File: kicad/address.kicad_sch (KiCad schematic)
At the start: 11 parts, among them J1 VLB_slot, U1 86C325, U8 7404, U9 7408

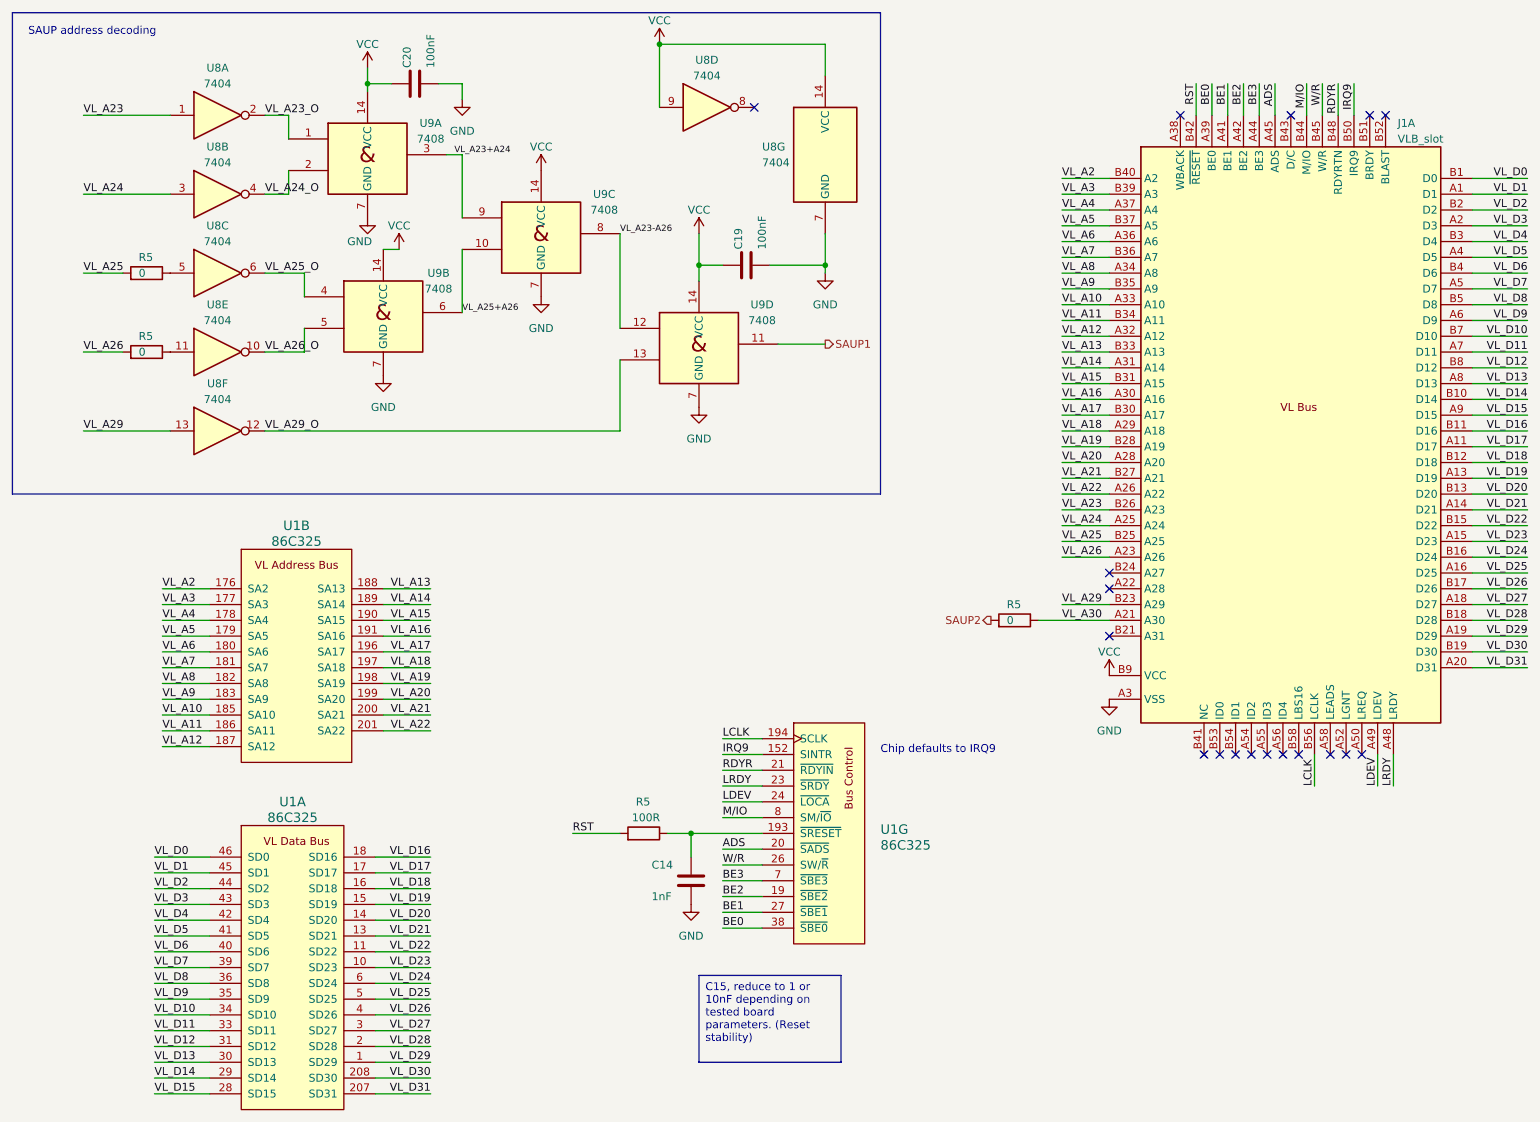
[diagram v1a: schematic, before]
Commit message: some optimizations and silkscreen updating
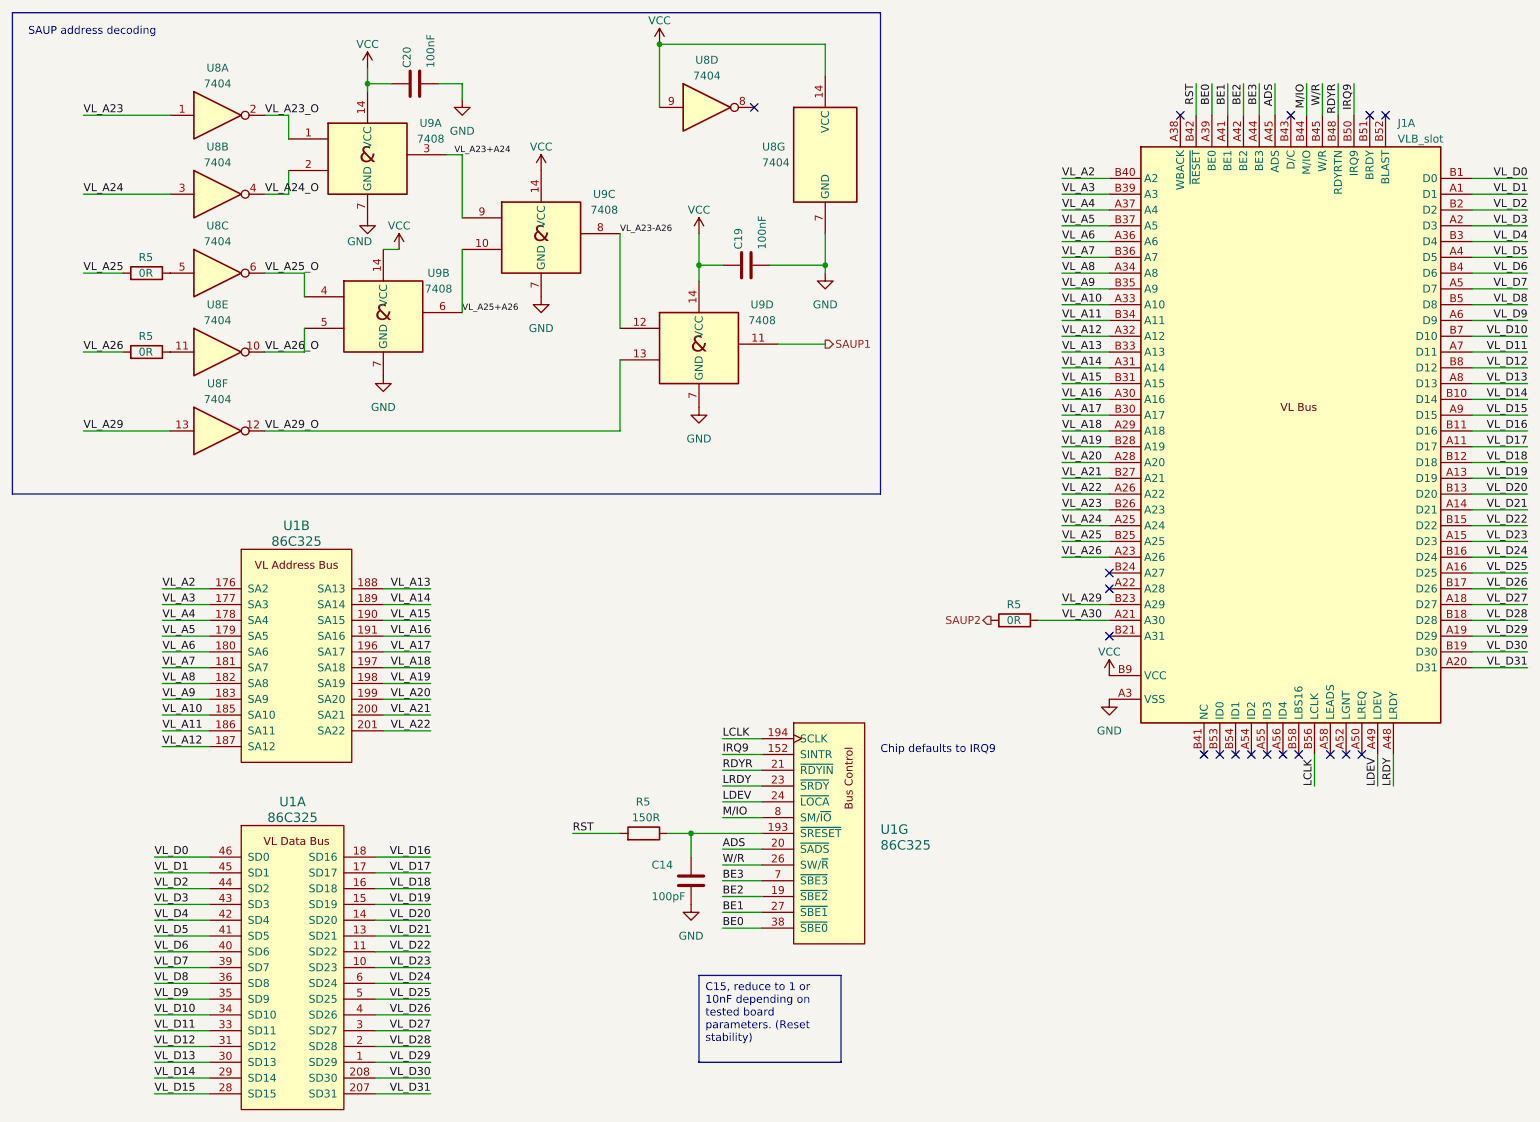
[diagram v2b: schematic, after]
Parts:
- C14: value 1nF -> 100pF
- J1: now left out of the parts list
- R5: value 100R -> 150R
- R5: value 0 -> 0R
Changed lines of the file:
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@@
       (effects (font (size 1.27 1.27)) (justify left))
     )
-    (property "Value" "100R" (at 116.205 144.78 90)
+    (property "Value" "150R" (at 116.205 144.78 90)
       (effects (font (size 1.27 1.27)) (justify left))
     )
@@
         )
         (path "/e8216711-86b5-4276-82f4-4c7ed22b9a9c/9321f466-5ac6-411a-b039-07fb7f0cdeaa"
-          (reference "R45") (unit 1)
+          (reference "R47") (unit 1)
         )
       )
@@
       (effects (font (size 1.27 1.27)) (justify left))
     )
-    (property "Value" "0" (at 36.83 69.85 90)
+    (property "Value" "0R" (at 36.83 69.85 90)
       (effects (font (size 1.27 1.27)) (justify left))
     )
@@
         )
         (path "/e8216711-86b5-4276-82f4-4c7ed22b9a9c/9321f466-5ac6-411a-b039-07fb7f0cdeaa"
-          (reference "R48") (unit 1)
+          (reference "R7") (unit 1)
         )
       )
@@
       (effects (font (size 1.27 1.27)) (justify left))
     )
-    (property "Value" "0" (at 36.83 57.15 90)
+    (property "Value" "0R" (at 36.83 57.15 90)
       (effects (font (size 1.27 1.27)) (justify left))
     )
@@
         )
         (path "/e8216711-86b5-4276-82f4-4c7ed22b9a9c/9321f466-5ac6-411a-b039-07fb7f0cdeaa"
-          (reference "R47") (unit 1)
+          (reference "R6") (unit 1)
         )
       )
@@
       (effects (font (size 1.27 1.27)) (justify left))
     )
-    (property "Value" "1nF" (at 119.38 157.48 0)
+    (property "Value" "100pF" (at 119.38 157.48 0)
       (effects (font (size 1.27 1.27)) (justify left))
     )
@@
       (effects (font (size 1.27 1.27)) (justify left))
     )
-    (property "Value" "0" (at 176.53 113.03 90)
+    (property "Value" "0R" (at 176.53 113.03 90)
       (effects (font (size 1.27 1.27)) (justify left))
     )
@@
         )
         (path "/e8216711-86b5-4276-82f4-4c7ed22b9a9c/9321f466-5ac6-411a-b039-07fb7f0cdeaa"
-          (reference "R49") (unit 1)
+          (reference "R8") (unit 1)
         )
       )
@@
   )
   (symbol (lib_id "virge:VLB_slot") (at 219.71 77.47 0) (unit 1)
-    (in_bom yes) (on_board yes) (dnp no)
+    (in_bom no) (on_board yes) (dnp no)
     (property "Reference" "J1" (at 239.4459 33.02 0)
       (effects (font (size 1.27 1.27)) (justify left))

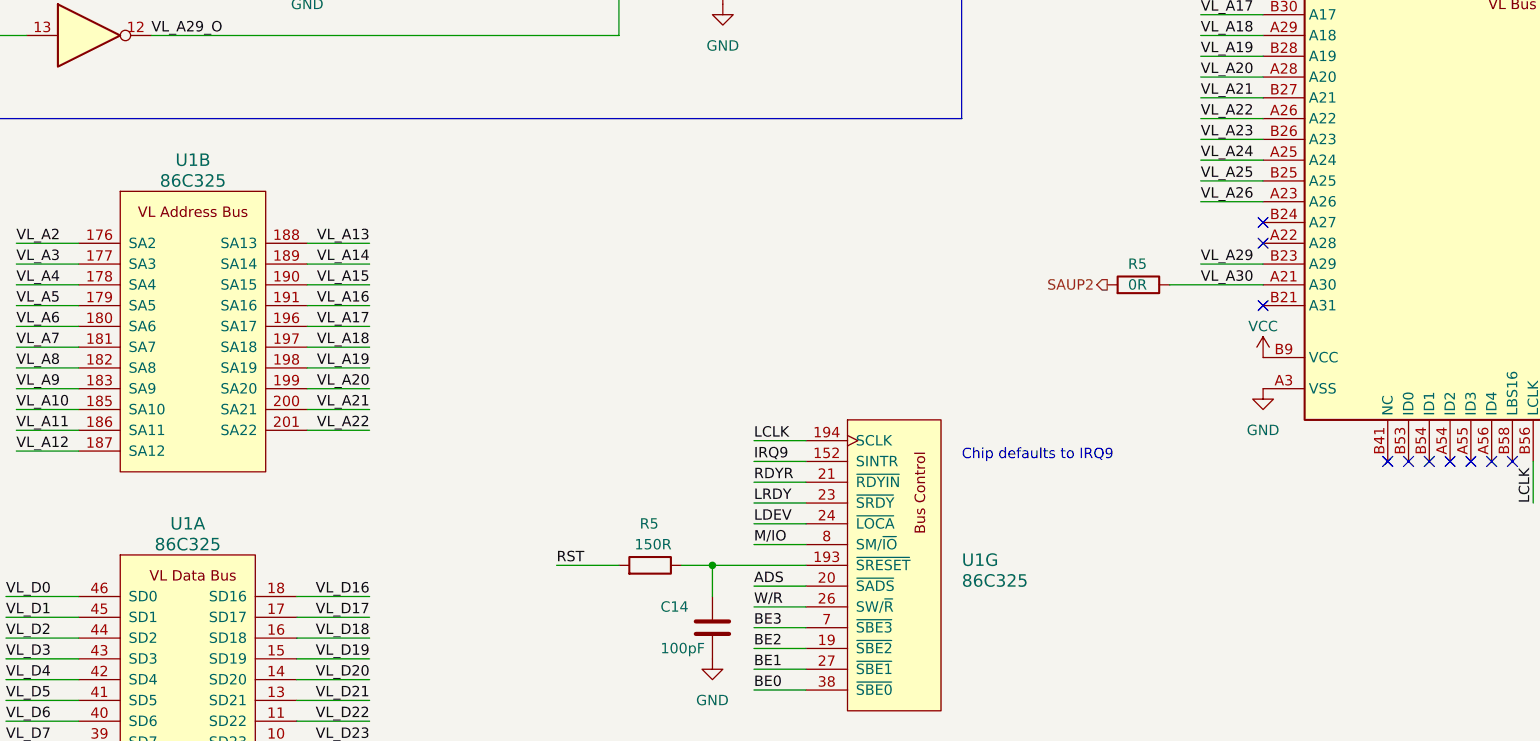
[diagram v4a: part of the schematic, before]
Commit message: updated VLB footprint
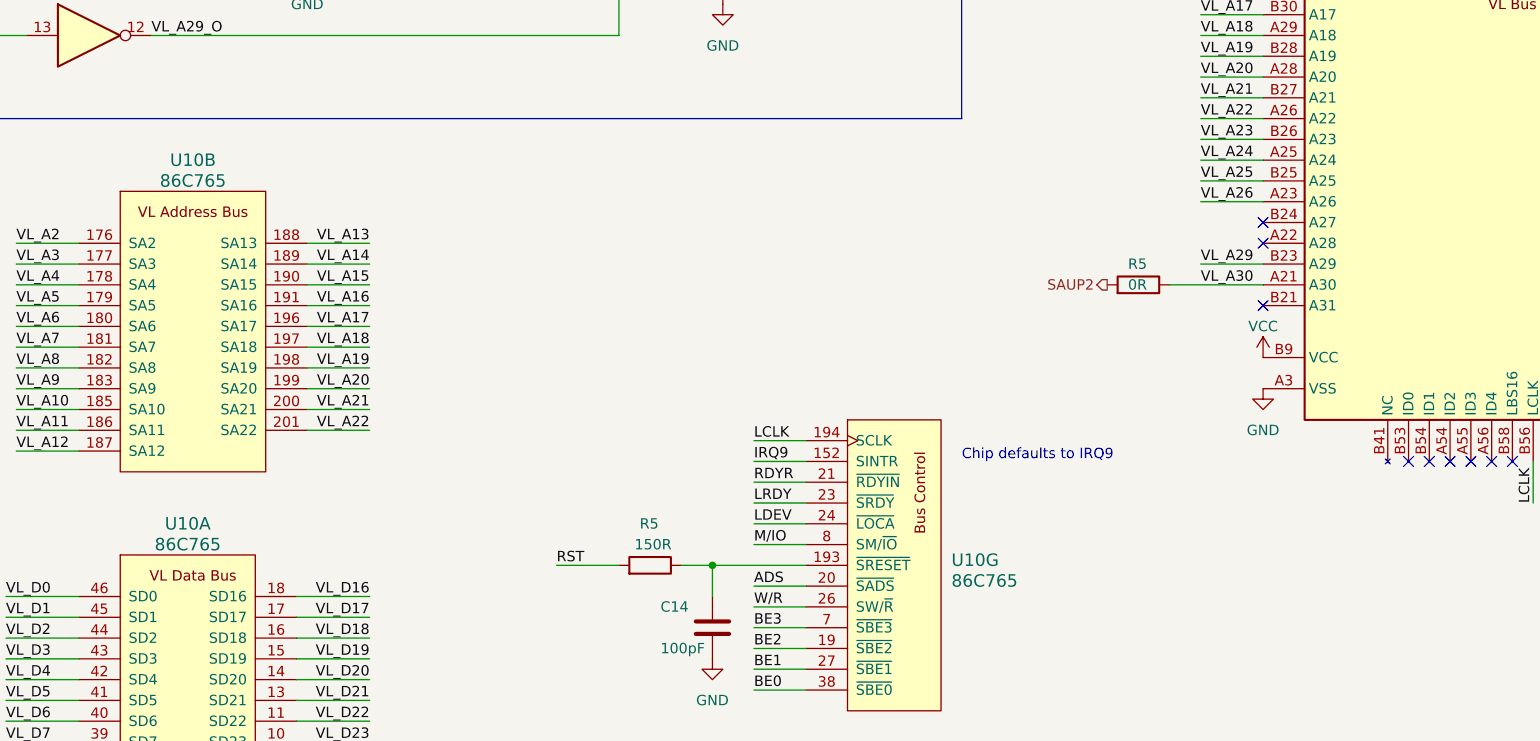
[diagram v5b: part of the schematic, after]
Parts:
- removed U1: 86C325, VLB:QFP-208, symbol virge:86C375
- added U10: 86C765, Package_QFP:PQFP-208_28x28mm_P0.5mm, symbol virge:86C765
- J1: footprint VLB:BUS_VLB_Board -> (none); now in the parts list
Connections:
- net ADS: now also U10.20 (~{SADS})
- net BE0: now also U10.38 (~{SBE0})
- net BE1: now also U10.27 (~{SBE1})
- net BE2: now also U10.19 (~{SBE2})
- net BE3: now also U10.7 (~{SBE3})
- net IRQ9: now also U10.152 (SINTR)
- net LCLK: now also U10.194 (SCLK)
- net LDEV: now also U10.24 (~{LOCA})
- net LRDY: now also U10.23 (~{SRDY})
- net M/IO: now also U10.8 (SM/~{IO})
- net RDYR: now also U10.21 (~{RDYIN})
- net VL_A10: now also U10.185 (SA10)
- net VL_A11: now also U10.186 (SA11)
- net VL_A12: now also U10.187 (SA12)
- net VL_A13: now also U10.188 (SA13)
- net VL_A14: now also U10.189 (SA14)
- net VL_A15: now also U10.190 (SA15)
- net VL_A16: now also U10.191 (SA16)
- net VL_A17: now also U10.196 (SA17)
- net VL_A18: now also U10.197 (SA18)
- net VL_A19: now also U10.198 (SA19)
- net VL_A2: now also U10.176 (SA2)
- net VL_A20: now also U10.199 (SA20)
- net VL_A21: now also U10.200 (SA21)
- net VL_A22: now also U10.201 (SA22)
- net VL_A3: now also U10.177 (SA3)
- net VL_A4: now also U10.178 (SA4)
- net VL_A5: now also U10.179 (SA5)
- net VL_A6: now also U10.180 (SA6)
- net VL_A7: now also U10.181 (SA7)
- net VL_A8: now also U10.182 (SA8)
- net VL_A9: now also U10.183 (SA9)
- net VL_D0: now also U10.46 (SD0)
- net VL_D1: now also U10.45 (SD1)
- net VL_D10: now also U10.34 (SD10)
- net VL_D11: now also U10.33 (SD11)
- net VL_D12: now also U10.31 (SD12)
- net VL_D13: now also U10.30 (SD13)
- net VL_D14: now also U10.29 (SD14)
- net VL_D15: now also U10.28 (SD15)
- net VL_D16: now also U10.18 (SD16)
- net VL_D17: now also U10.17 (SD17)
- net VL_D18: now also U10.16 (SD18)
- net VL_D19: now also U10.15 (SD19)
- net VL_D2: now also U10.44 (SD2)
- net VL_D20: now also U10.14 (SD20)
- net VL_D21: now also U10.13 (SD21)
- net VL_D22: now also U10.11 (SD22)
- net VL_D23: now also U10.10 (SD23)
- net VL_D24: now also U10.6 (SD24)
- net VL_D25: now also U10.5 (SD25)
- net VL_D26: now also U10.4 (SD26)
- net VL_D27: now also U10.3 (SD27)
- net VL_D28: now also U10.2 (SD28)
- net VL_D29: now also U10.1 (SD29)
- net VL_D3: now also U10.43 (SD3)
- net VL_D30: now also U10.208 (SD30)
- net VL_D31: now also U10.207 (SD31)
- net VL_D4: now also U10.42 (SD4)
- net VL_D5: now also U10.41 (SD5)
- net VL_D6: now also U10.40 (SD6)
- net VL_D7: now also U10.39 (SD7)
- net VL_D8: now also U10.36 (SD8)
- net VL_D9: now also U10.35 (SD9)
- net W/R: now also U10.26 (SW/~{R})
- net at C14.1, R5.1: now also U10.193 (~{SRESET})
- no-connect marks 18 -> 17

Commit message: fixed VGA footprint
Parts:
- J1: footprint (none) -> VLB:BUS_VLB_Board
- U10: footprint Package_QFP:PQFP-208_28x28mm_P0.5mm -> VLB:QFP-208
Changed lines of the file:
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@@
       (effects (font (size 1.524 1.524)) (justify left))
     )
-    (property "Footprint" "Package_QFP:PQFP-208_28x28mm_P0.5mm" (at 107.95 142.24 0)
+    (property "Footprint" "VLB:QFP-208" (at 107.95 142.24 0)
       (effects (font (size 1.524 1.524)) (justify right) hide)
     )
@@
       (effects (font (size 1.524 1.524)))
     )
-    (property "Footprint" "Package_QFP:PQFP-208_28x28mm_P0.5mm" (at 20.32 115.57 0)
+    (property "Footprint" "VLB:QFP-208" (at 20.32 115.57 0)
       (effects (font (size 1.524 1.524)) (justify right) hide)
     )
@@
       (effects (font (size 1.524 1.524)))
     )
-    (property "Footprint" "Package_QFP:PQFP-208_28x28mm_P0.5mm" (at 21.59 165.1 0)
+    (property "Footprint" "VLB:QFP-208" (at 21.59 165.1 0)
       (effects (font (size 1.524 1.524)) (justify right) hide)
     )
@@
       (effects (font (size 1.27 1.27)) (justify left))
     )
-    (property "Footprint" "" (at 184.15 62.23 0)
-      (effects (font (size 1.27 1.27)) hide)
-    )
+    (property "Footprint" "VLB:BUS_VLB_Board" (at 184.15 62.23 0)
+      (effects (font (size 1.27 1.27)) hide)
+    )

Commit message: final fixes
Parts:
- added JP3: Conn_01x03, Connector_PinHeader_2.54mm:PinHeader_1x03_P2.54mm_Vertical, symbol Connector_Generic:Conn_01x03
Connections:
- net IRQ9: now also JP3.1 (Pin_1); no longer U10.152 (SINTR)
- new net: JP3.2 (Pin_2), U10.152 (SINTR)
- no-connect marks 17 -> 18
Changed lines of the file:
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@@
   (no_connect (at 210.82 134.62))
   (no_connect (at 222.25 31.75))
+  (no_connect (at 120.65 137.16))
   (no_connect (at 215.9 134.62))
   (wire (pts (xy 185.42 77.47) (xy 193.04 77.47))
@@
     (stroke (width 0) (type default))
   )
+  (wire (pts (xy 137.16 134.62) (xy 120.65 134.62))
+    (stroke (width 0) (type default))
+  )
   (wire (pts (xy 125.73 147.32) (xy 125.73 151.13))
     (stroke (width 0) (type default))
@@
     (stroke (width 0) (type default))
   )
+  (wire (pts (xy 120.65 132.08) (xy 125.73 132.08))
+    (stroke (width 0) (type default))
+  )
   (wire (pts (xy 251.46 44.45) (xy 260.35 44.45))
     (stroke (width 0) (type default))
@@
   )
   (wire (pts (xy 251.46 97.79) (xy 260.35 97.79))
-    (stroke (width 0) (type default))
-  )
-  (wire (pts (xy 130.81 134.62) (xy 137.16 134.62))
     (stroke (width 0) (type default))
   )
@@
     (effects (font (size 1.27 1.27)) (justify left bottom))
   )
-  (label "IRQ9" (at 130.81 134.62 0) (fields_autoplaced)
-    (effects (font (size 1.27 1.27)) (justify left bottom))
-  )
   (label "VL_A13" (at 83.82 107.95 180) (fields_autoplaced)
     (effects (font (size 1.27 1.27)) (justify right bottom))
@@
   )
   (label "VL_A14" (at 83.82 110.49 180) (fields_autoplaced)
+    (effects (font (size 1.27 1.27)) (justify right bottom))
+  )
+  (label "IRQ9" (at 125.73 132.08 180) (fields_autoplaced)
     (effects (font (size 1.27 1.27)) (justify right bottom))
   )
@@
         )
       )
+    )
+  )
+  (symbol (lib_id "Connector_Generic:Conn_01x03") (at 115.57 134.62 0) (mirror y) (unit 1)
+    (in_bom yes) (on_board yes) (dnp no)
+    (property "Reference" "JP3" (at 113.03 133.35 0)
+      (effects (font (size 1.27 1.27)) (justify left))
+    )
+    (property "Value" "Conn_01x03" (at 113.03 135.89 0)
+      (effects (font (size 1.27 1.27)) (justify left) hide)
+    )
+    (property "Footprint" "Connector_PinHeader_2.54mm:PinHeader_1x03_P2.54mm_Vertical" (at 115.57 134.62 0)
+      (effects (font (size 1.27 1.27)) hide)
+    )
+    (property "Datasheet" "~" (at 115.57 134.62 0)
+      (effects (font (size 1.27 1.27)) hide)
+    )
+    (pin "1")
+    (pin "2")
+    (pin "3")
+    (instances
+      (project "virge-vlb"
+        (path "/e8216711-86b5-4276-82f4-4c7ed22b9a9c/485e825d-a3d2-4e3d-9ea7-d005dd511bf5"
+          (reference "JP3") (unit 1)
+        )
+        (path "/e8216711-86b5-4276-82f4-4c7ed22b9a9c/9321f466-5ac6-411a-b039-07fb7f0cdeaa"
+          (reference "JP4") (unit 1)
+        )
+      )
